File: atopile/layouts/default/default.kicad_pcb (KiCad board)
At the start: 4 copper layers, 78 x 60 mm, 86 parts

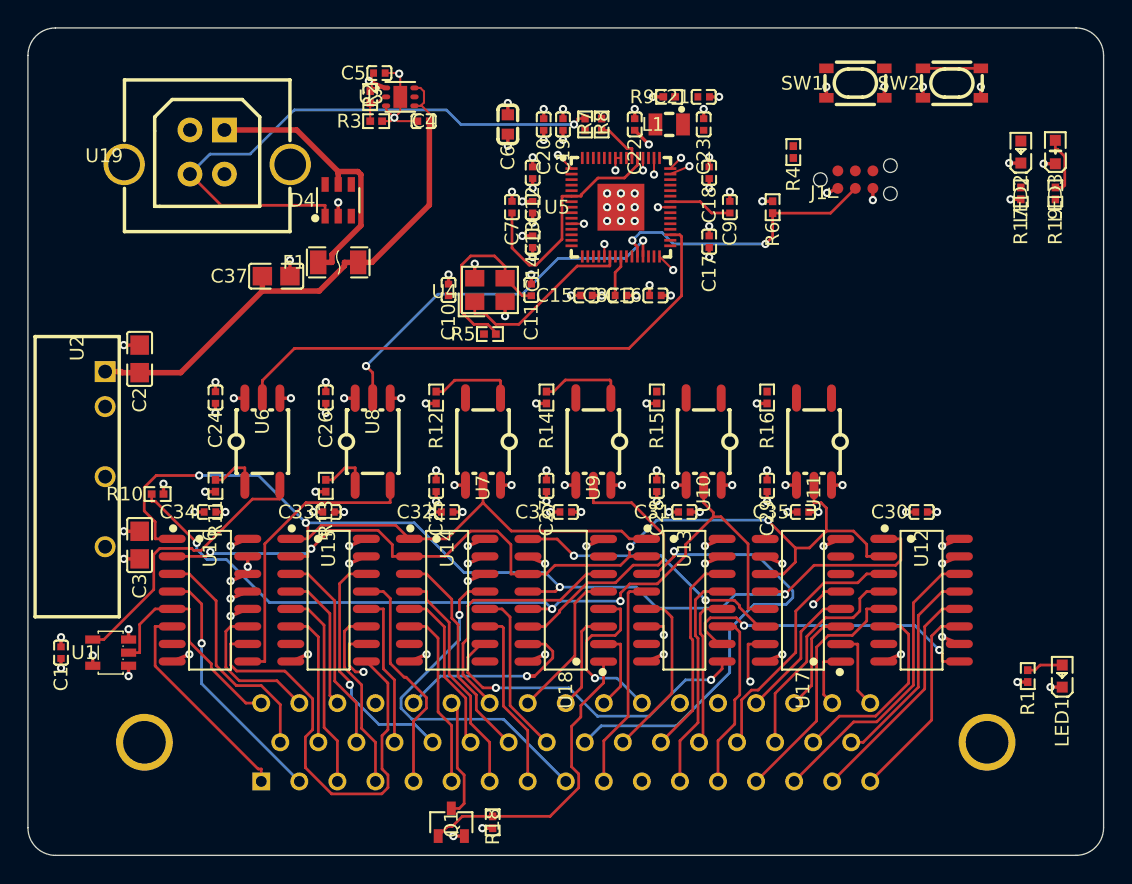
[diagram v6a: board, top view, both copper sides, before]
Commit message: atopile: Freerouting patch saves the final board; VREG_LX no-via area
- freerouting-2.1.0-cli-output.patch (was -timeout.patch): also save the
  session after the router restores its best board; before, the .ses was
  a mid-pass snapshot (KiCad found up to 30 open connections where
  Freerouting reported 3)
- plane_vias.py: no-via area on the VREG_LX path (RP2354A pin 48 to L1);
  a +3V3 drop there had blocked it
Layout reset to the new via drops, unrouted, for the next run.

Co-Authored-By: Claude Opus 5.5 <noreply@anthropic.com>
Claude-Session: https://claude.ai/code/session_01NqBEt2iCuw3VMJkgzgPtpr
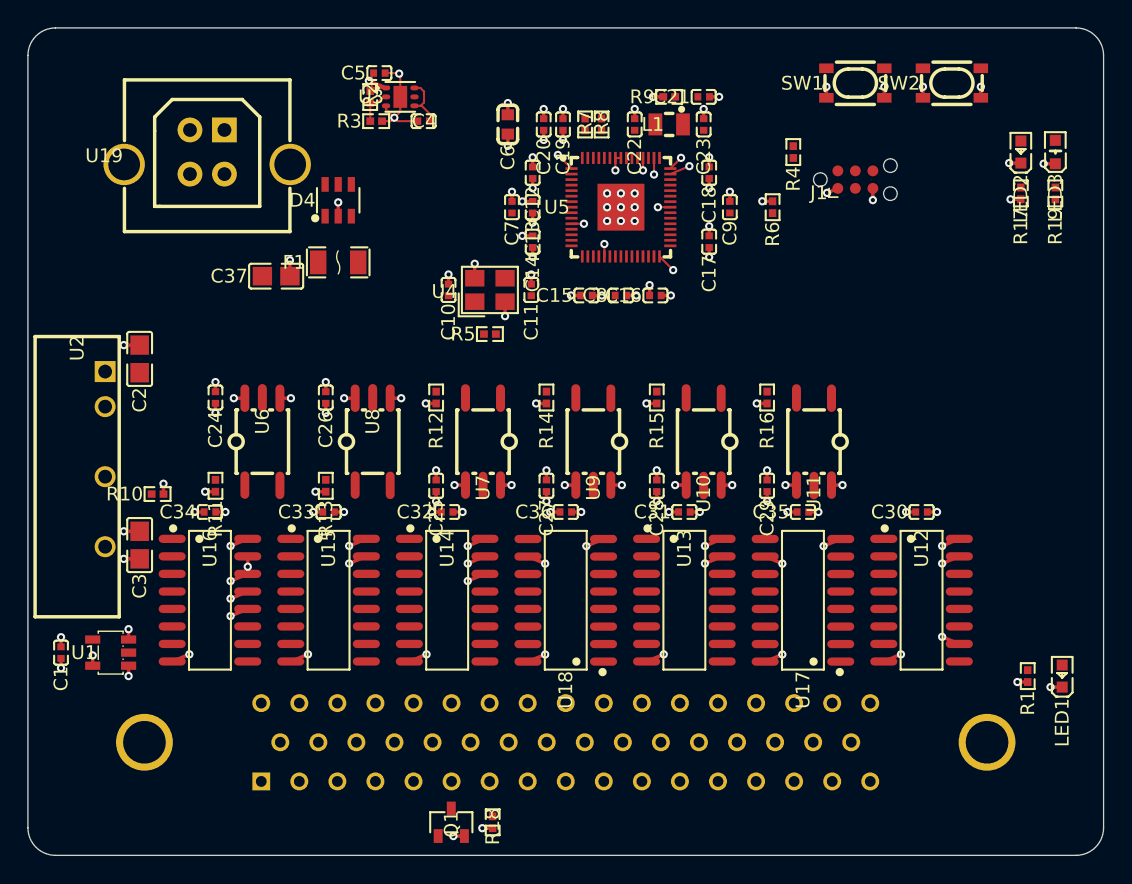
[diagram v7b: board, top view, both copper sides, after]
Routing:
- net LATCH_ISO: track 103.9 -> 0.00 mm, vias 4 -> 0
- net SCK_ISO: track 72.6 -> 0.00 mm, vias 4 -> 0
- net OE_N_ISO: track 61.9 -> 0.00 mm, vias 3 -> 0
- net DATA_P: track 42.8 -> 0.00 mm, vias 1 -> 0
- net DRDY: track 39.4 -> 0.00 mm
- net +5V: track 39.9 -> 3.86 mm
- net SKB26_POL_POS: track 35.9 -> 0.00 mm, vias 1 -> 0
- net SI_CHAIN_1: track 32.0 -> 0.00 mm
- net MISO: track 27.5 -> 0.00 mm, vias 2 -> 0
- net SKB09_D4_1: track 25.8 -> 0.00 mm, vias 1 -> 0
- net +1V1: track 25.2 -> 0.00 mm
- net N_RESET: track 24.9 -> 0.00 mm, vias 2 -> 0
- net SI_CHAIN_3: track 24.9 -> 0.00 mm, vias 2 -> 0
- net SI_CHAIN_4: track 22.4 -> 0.00 mm, vias 2 -> 0
- net SAMPLE_CONTACT_GATE: track 22.0 -> 0.00 mm
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
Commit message: atopile: board fully routed on 4 layers; fab outputs and README
- layout: Freerouting run 10 (patched 2.1, plane via drops, no-via areas)
  plus finish_routes.py for the last 2 connections; KiCad DRC: 0 errors,
  0 unrouted (warnings: silkscreen, J1 footprint mismatch)
- fab/: gerbers now include In1.Cu/In2.Cu, zip no longer _UNROUTED_,
  prints add the two plane layers, renders and DRC report regenerated
- finish_routes.py: name pads by reference+number (pads of identical
  footprints share UUIDs, which merged split nets)
- import_routing.py: --clear
- README: "Planes and routing" section with the run-by-run table, routed
  board figure, updated outputs and open items; placement figure updated

Co-Authored-By: Claude Opus 5.5 <noreply@anthropic.com>
Claude-Session: https://claude.ai/code/session_01NqBEt2iCuw3VMJkgzgPtpr
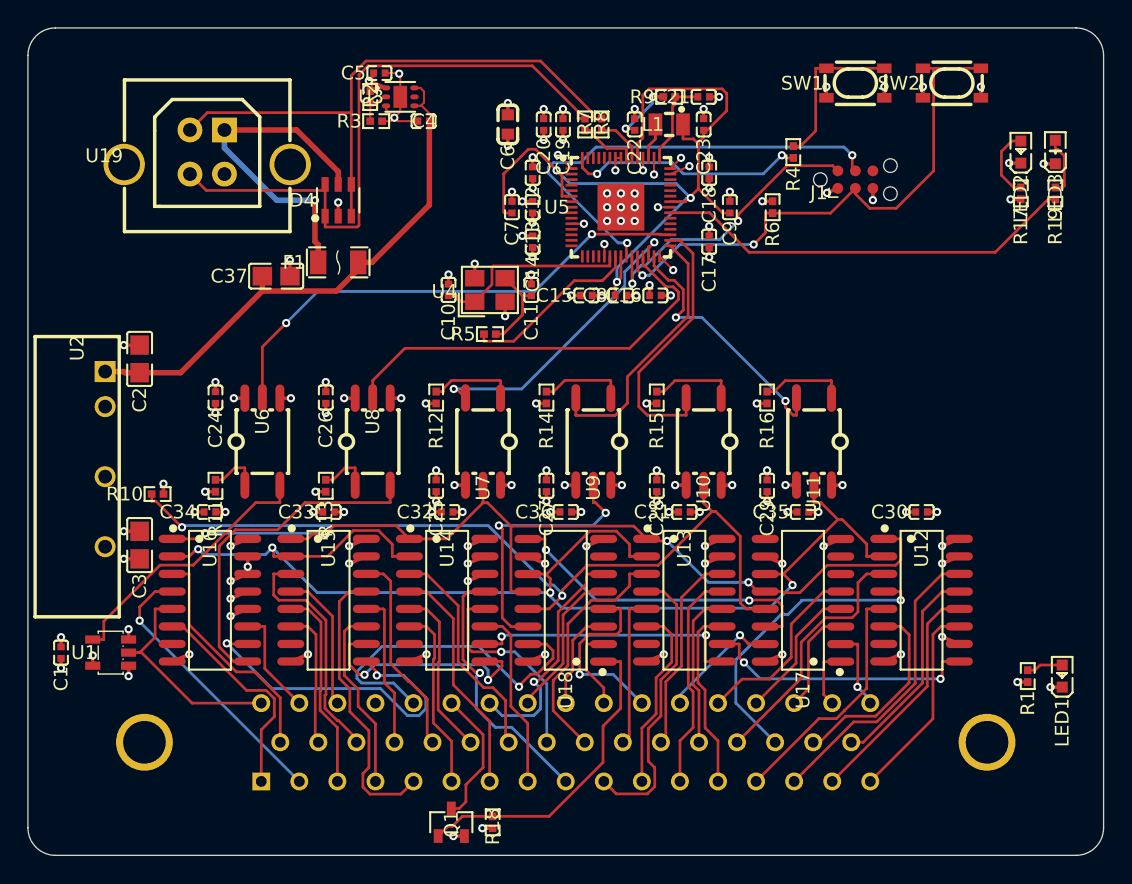
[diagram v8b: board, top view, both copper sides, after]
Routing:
- net SCK_ISO: track 0.00 -> 89.9 mm, vias 0 -> 4
- net LATCH_ISO: track 0.00 -> 69.2 mm, vias 0 -> 4
- net OE_N_ISO: track 0.00 -> 61.6 mm, vias 0 -> 2
- net +1V1: track 0.00 -> 60.3 mm, vias 0 -> 3
- net DATA_P: track 0.00 -> 45.4 mm
- net DATA_N: track 0.00 -> 42.9 mm
- net N_RESET: track 0.00 -> 39.7 mm, vias 0 -> 2
- net DRDY: track 0.00 -> 36.7 mm, vias 0 -> 2
- net +5V: track 3.86 -> 40.2 mm
- net CLK: track 0.00 -> 33.3 mm, vias 0 -> 2
- net STATUS_LED: track 0.00 -> 30.7 mm
- net MISO: track 0.00 -> 30.4 mm
- net SKB38_LOCKOUT: track 0.00 -> 25.0 mm, vias 0 -> 1
- net MISO_ISO: track 0.00 -> 24.8 mm
- net SI_CHAIN_1: track 0.00 -> 24.7 mm, vias 0 -> 2
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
